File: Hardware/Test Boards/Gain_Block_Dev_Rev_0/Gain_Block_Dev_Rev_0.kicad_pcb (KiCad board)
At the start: 2 copper layers, 48 x 48 mm, 48 parts, among them J1 USB_B_Micro, J2 RF_IN, J3 Conn_02x03_Odd_Even, J4 RF_OUT, SW1 SW_DIP_x08, U1 PE43711, U2 AMS1117-3.3, U3 LP5907MFX-3.3, U4 AD8319, U5 HMC313

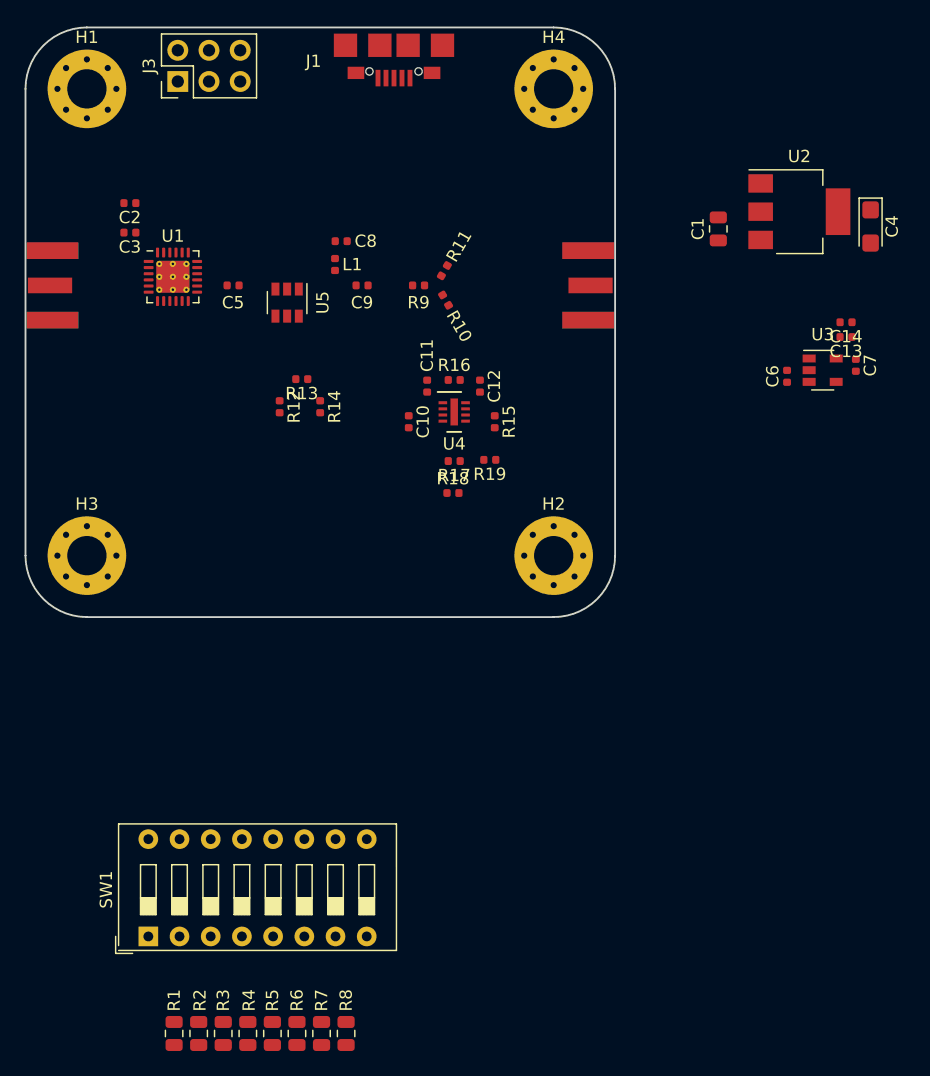
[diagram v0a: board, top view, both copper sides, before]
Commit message: Changed coupler to 4 layer board, turned gerbers into panel, made BOM spreadsheet.
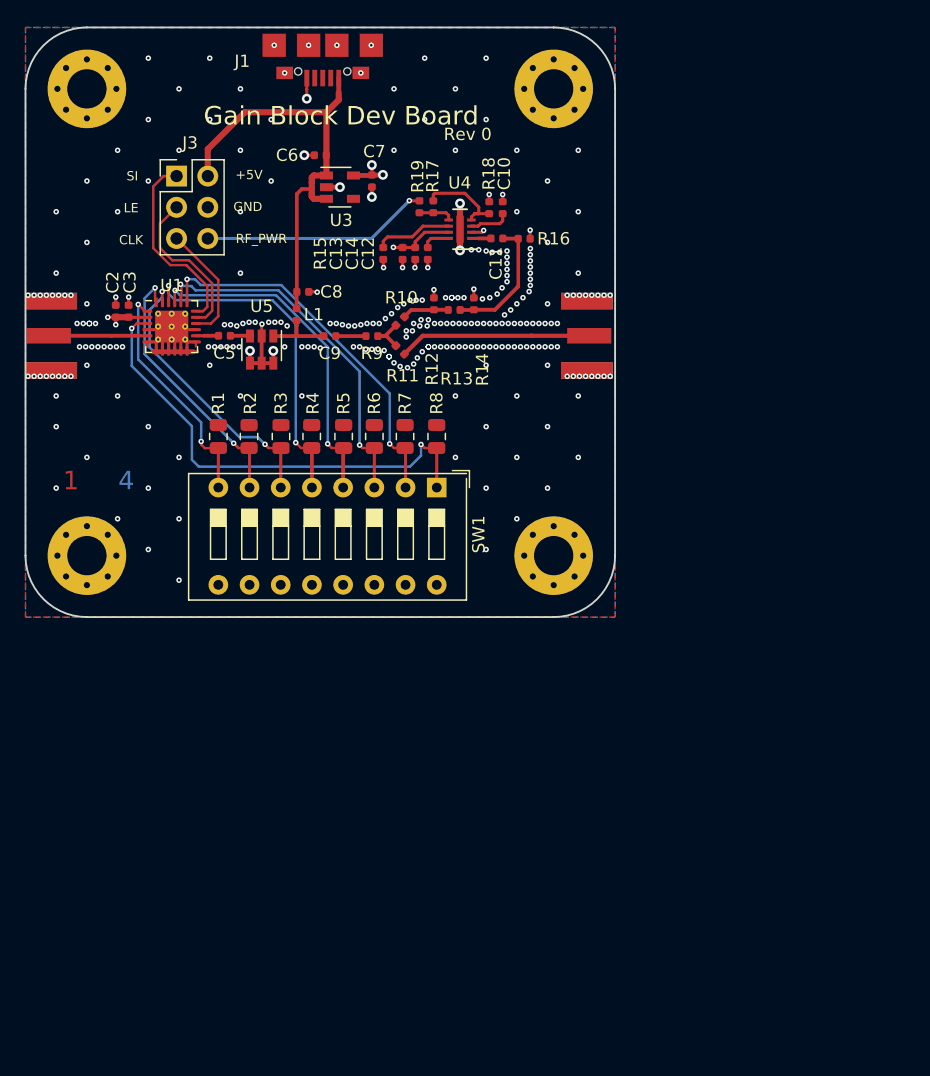
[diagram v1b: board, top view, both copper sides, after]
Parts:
- removed C1: 10u, Capacitor_SMD:C_0805_2012Metric
- removed C4: 22u, Capacitor_Tantalum_SMD:CP_EIA-3216-18_Kemet-A
- removed U2: AMS1117-3.3, Package_TO_SOT_SMD:SOT-223-3_TabPin2
- added G***: LOGO, VNA_Footprints:OSHW_Logo_3.6x3.6_F.Mask, F.Cu at (110.9, 103.3)
- added REF**: Board Title, VNA_Footprints:BoardTitle, F.Cu at (134.0, 75.0)
- added REF**: Josh Details, VNA_Footprints:JoshDetails, B.Cu at (139.1, 111.2)
- added REF**: 4LayerCheck, VNA_Footprints:4LayerCheck, F.Cu at (111.2, 106.9)
- U1: footprint Package_DFN_QFN:QFN-24-1EP_4x4mm_P0.5mm_EP2.7x2.6mm_ThermalVias -> VNA_Footprints:QFN-24-1EP_4x4mm_P0.5mm_EP2.7x2.6mm_ThermalVias
- moved R8 49.2 mm to (138.5, 103.3)
- moved R7 49.1 mm to (135.9, 103.3)
- moved R6 49.0 mm to (133.4, 103.3)
- moved R5 48.9 mm to (130.9, 103.3)
- moved R4 48.9 mm to (128.3, 103.3)
- moved R3 48.8 mm to (125.8, 103.3)
- moved R2 48.8 mm to (123.2, 103.3)
- moved R1 48.7 mm to (120.7, 103.3)
- moved SW1 43.4 mm to (138.5, 107.5), turned to 270 degrees
- moved C7 42.2 mm to (133.2, 82.5)
- moved C6 42.0 mm to (129.0, 80.4), turned to 180 degrees
- moved U3 42.0 mm to (130.6, 83.0)
- moved C13 36.7 mm to (135.7, 88.4), turned to 90 degrees
- moved C14 35.5 mm to (136.7, 88.4), turned to 90 degrees
- moved R18 23.4 mm to (142.8, 84.7), turned to 90 degrees
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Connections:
- J3 pad 4: /RF_PWR -> GND
- J3 pad 6: GND -> /RF_PWR
- SW1 pad 1: +3V3 -> /nP_S
- SW1 pad 10: Net-(R7-Pad1) -> +3.3VA
- SW1 pad 11: Net-(R6-Pad1) -> +3.3VA
- SW1 pad 12: Net-(R5-Pad1) -> +3.3VA
- SW1 pad 13: Net-(R4-Pad1) -> +3.3VA
- SW1 pad 14: Net-(R3-Pad1) -> +3.3VA
- SW1 pad 15: Net-(R2-Pad1) -> +3.3VA
- SW1 pad 16: Net-(R1-Pad1) -> +3.3VA
- SW1 pad 2: +3V3 -> Net-(R7-Pad1)
- SW1 pad 3: +3V3 -> Net-(R6-Pad1)
- SW1 pad 4: +3V3 -> Net-(R5-Pad1)
- SW1 pad 5: +3V3 -> Net-(R4-Pad1)
- SW1 pad 6: +3V3 -> Net-(R3-Pad1)
- SW1 pad 7: +3V3 -> Net-(R2-Pad1)
- SW1 pad 8: +3V3 -> Net-(R1-Pad1)
- SW1 pad 9: /nP_S -> +3.3VA
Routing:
- net GND: track 0.00 -> 47.4 mm, vias 0 -> 278
- net /nP_S: track 0.00 -> 38.9 mm, vias 0 -> 2
- net +5V: track 0.00 -> 37.5 mm
- net Net-(R7-Pad1): track 0.00 -> 31.1 mm, vias 0 -> 2
- net Net-(R6-Pad1): track 0.00 -> 29.6 mm, vias 0 -> 2
- net Net-(R4-Pad1): track 0.00 -> 28.3 mm, vias 0 -> 2
- net Net-(R5-Pad1): track 0.00 -> 28.2 mm, vias 0 -> 2
- net Net-(R3-Pad1): track 0.00 -> 23.2 mm, vias 0 -> 2
- net Net-(R2-Pad1): track 0.00 -> 21.9 mm, vias 0 -> 2
- net Net-(R1-Pad1): track 0.00 -> 19.9 mm, vias 0 -> 2
- net /RF_PWR: track 0.00 -> 18.5 mm, vias 0 -> 1
- net /SI: track 0.00 -> 15.7 mm
- net Net-(J4-Pad1): track 0.00 -> 15.7 mm
- net /LE: track 0.00 -> 13.1 mm
- net +3.3VA: track 0.00 -> 12.4 mm, vias 0 -> 5
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- added copper zone on In2.Cu, net +3.3VA
- added copper zone on B.Cu, net GND
- added copper zone on F.Cu, net GND
- added copper zone on In1.Cu, net GND
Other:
- copper layers 2 -> 4
- net class Default: clearance 0.2 -> 0.1
- rule trace_clearance: 0.2 -> 0.1
- rule trace_min: 0.2 -> 0.15
- rule via_min_drill: 0.3 -> 0.2
- rule via_min_size: 0.4 -> 0.45
- board text added: "+5V"
- board text added: "CLK"
- board text added: "GND"
- board text added: "LE"
- board text added: "RF_PWR"
- board text added: "SI"

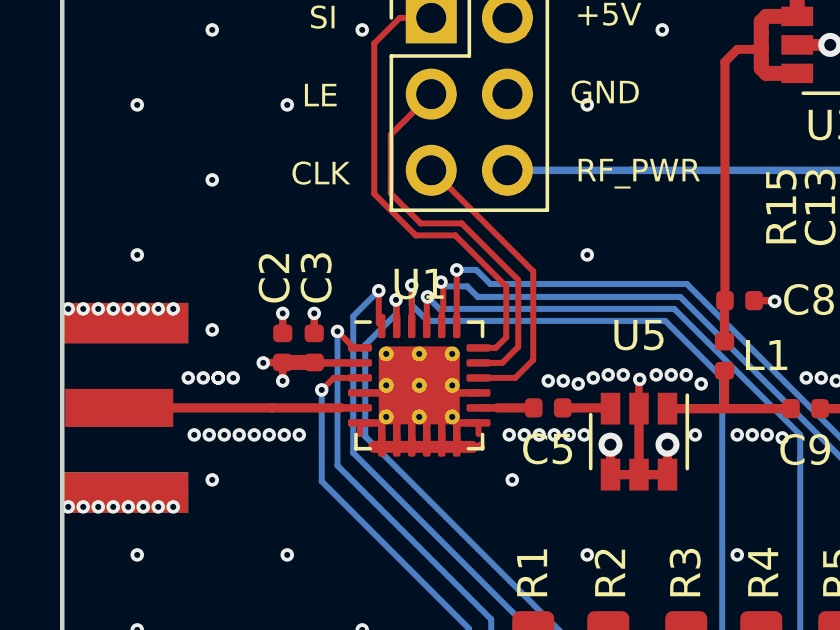
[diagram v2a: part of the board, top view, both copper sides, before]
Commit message: Changed R17 in gain block from OPT to 0R0
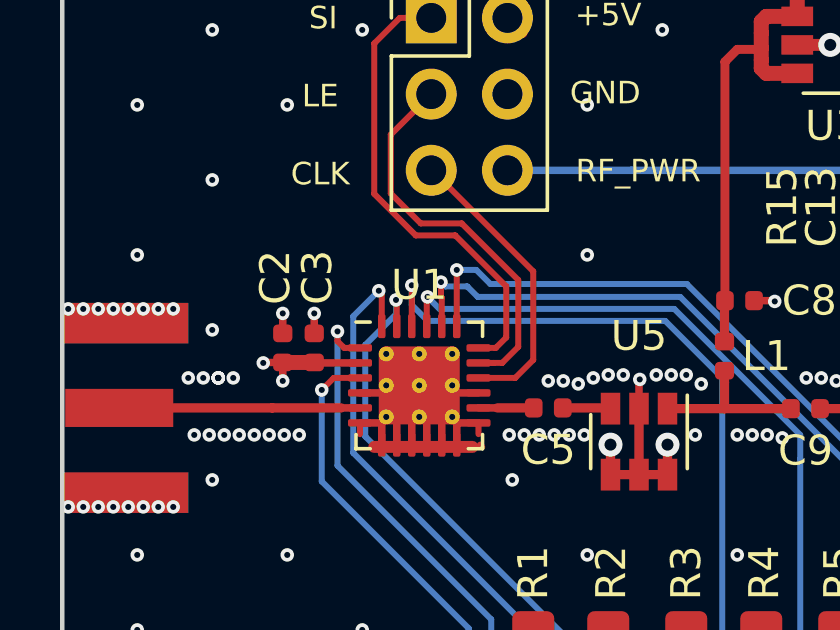
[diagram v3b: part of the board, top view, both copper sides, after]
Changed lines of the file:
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@@
     (thickness 1.6)
     (drawings 14)
-    (tracks 583)
+    (tracks 584)
     (zones 0)
     (modules 49)
@@
     (37 F.SilkS user hide)
     (38 B.Mask user hide)
-    (39 F.Mask user hide)
+    (39 F.Mask user)
     (40 Dwgs.User user hide)
     (41 Cmts.User user hide)
@@
   (segment (start 120.6625 104.2) (end 120.7 104.2375) (width 0.25) (layer F.Cu) (net 21))
   (via (at 114.17499 92.55) (size 0.45) (drill 0.2) (layers F.Cu B.Cu) (net 21))
-  (segment (start 114.925 93.1) (end 114.72499 93.1) (width 0.2) (layer F.Cu) (net 21))
-  (segment (start 114.72499 93.1) (end 114.17499 92.55) (width 0.2) (layer F.Cu) (net 21))
   (segment (start 120.6875 104.25) (end 120.7 104.2375) (width 0.2) (layer F.Cu) (net 21))
   (segment (start 120.7 106.32363) (end 120.7 104.2375) (width 0.25) (layer F.Cu) (net 21))
@@
   (segment (start 119.3 103.95) (end 119.6 104.25) (width 0.2) (layer F.Cu) (net 21))
   (segment (start 119.3 103.7) (end 119.3 102.15) (width 0.2) (layer B.Cu) (net 21))
+  (segment (start 114.17499 92.87499) (end 114.17499 92.55) (width 0.2) (layer F.Cu) (net 21))
+  (segment (start 114.925 93.1) (end 114.4 93.1) (width 0.2) (layer F.Cu) (net 21))
+  (segment (start 114.4 93.1) (end 114.17499 92.87499) (width 0.2) (layer F.Cu) (net 21))
   (segment (start 123.24 104.2775) (end 123.2 104.2375) (width 0.25) (layer F.Cu) (net 22))
   (segment (start 123.24 107.455) (end 123.24 104.2775) (width 0.25) (layer F.Cu) (net 22))
   (via (at 115.551468 91.194117) (size 0.45) (drill 0.2) (layers F.Cu B.Cu) (net 22))
-  (segment (start 115.65 92.375) (end 115.551468 92.276468) (width 0.2) (layer F.Cu) (net 22))
-  (segment (start 115.551468 92.276468) (end 115.551468 91.194117) (width 0.2) (layer F.Cu) (net 22))
   (segment (start 114.69999 92.045595) (end 114.69999 96.599934) (width 0.2) (layer B.Cu) (net 22))
   (segment (start 114.69999 96.599934) (end 121.725057 103.625001) (width 0.2) (layer B.Cu) (net 22))
@@
   (segment (start 115.551468 91.194117) (end 114.69999 92.045595) (width 0.2) (layer B.Cu) (net 22))
   (via (at 121.950056 103.85) (size 0.45) (drill 0.2) (layers F.Cu B.Cu) (net 22))
+  (segment (start 115.65 91.292649) (end 115.551468 91.194117) (width 0.2) (layer F.Cu) (net 22))
+  (segment (start 115.65 92.375) (end 115.65 91.292649) (width 0.2) (layer F.Cu) (net 22))
   (segment (start 125.78 104.2575) (end 125.8 104.2375) (width 0.25) (layer F.Cu) (net 23))
   (segment (start 125.78 107.455) (end 125.78 104.2575) (width 0.25) (layer F.Cu) (net 23))
@@
   (via (at 132.2 104) (size 0.45) (drill 0.2) (layers F.Cu B.Cu) (net 26))
   (via (at 117.625 90.906053) (size 0.45) (drill 0.2) (layers F.Cu B.Cu) (net 26))
-  (segment (start 117.65 92.375) (end 117.65 91.875) (width 0.2) (layer F.Cu) (net 26))
-  (segment (start 117.65 91.875) (end 117.700011 91.824989) (width 0.2) (layer F.Cu) (net 26))
-  (segment (start 117.700011 91.824989) (end 117.700011 90.981064) (width 0.2) (layer F.Cu) (net 26))
   (segment (start 117.700011 90.981064) (end 117.625 90.906053) (width 0.2) (layer F.Cu) (net 26))
   (segment (start 117.768947 91.05) (end 117.625 90.906053) (width 0.2) (layer B.Cu) (net 26))
@@
   (segment (start 132.2 104) (end 132.2 98) (width 0.2) (layer B.Cu) (net 26))
   (segment (start 132.2 98) (end 125.6 91.4) (width 0.2) (layer B.Cu) (net 26))
+  (segment (start 117.625 91.4) (end 117.625 90.906053) (width 0.2) (layer F.Cu) (net 26))
+  (segment (start 117.65 92.375) (end 117.65 91.425) (width 0.2) (layer F.Cu) (net 26))
+  (segment (start 117.65 91.425) (end 117.625 91.4) (width 0.2) (layer F.Cu) (net 26))
   (segment (start 135.94 104.2775) (end 135.9 104.2375) (width 0.25) (layer F.Cu) (net 27))
   (segment (start 135.94 107.455) (end 135.94 104.2775) (width 0.25) (layer F.Cu) (net 27))
